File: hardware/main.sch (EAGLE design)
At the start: 107 parts, among them IC1 MPU-6050, IC2 TB6612FNG, M1 MOTOR_MOUNT_V2, M2 LED_MOUNT, M3 LED_MOUNT, M4 LED_MOUNT, M5 LED_MOUNT, M6 LED_MOUNT, M7 LED_MOUNT, Q7 IRLML2244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

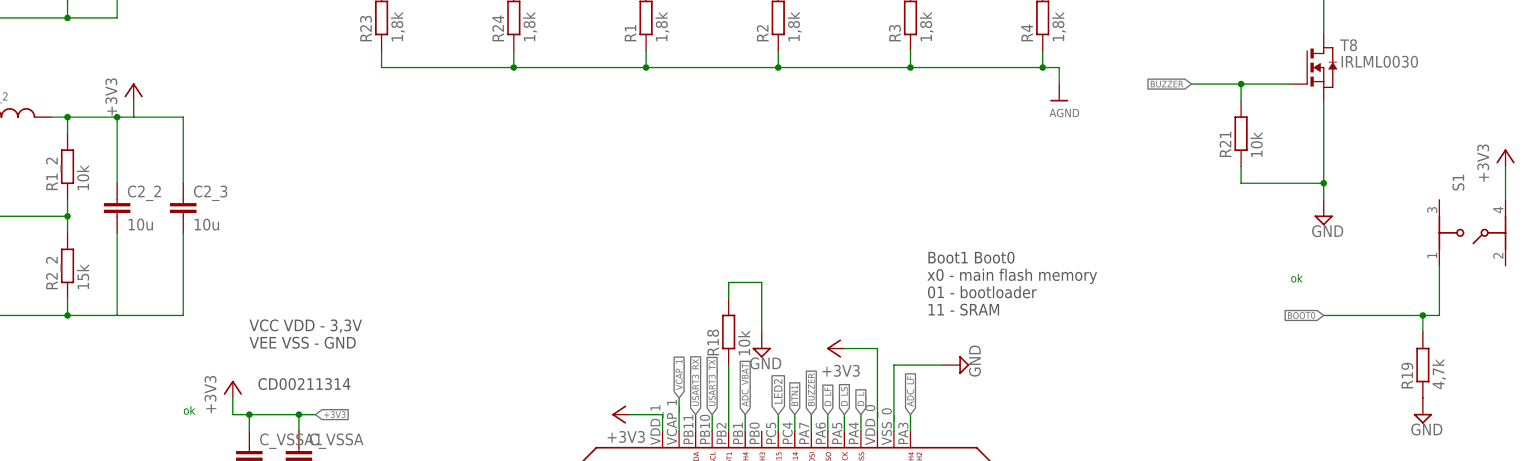
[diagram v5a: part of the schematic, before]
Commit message: pcb matches the 3d model
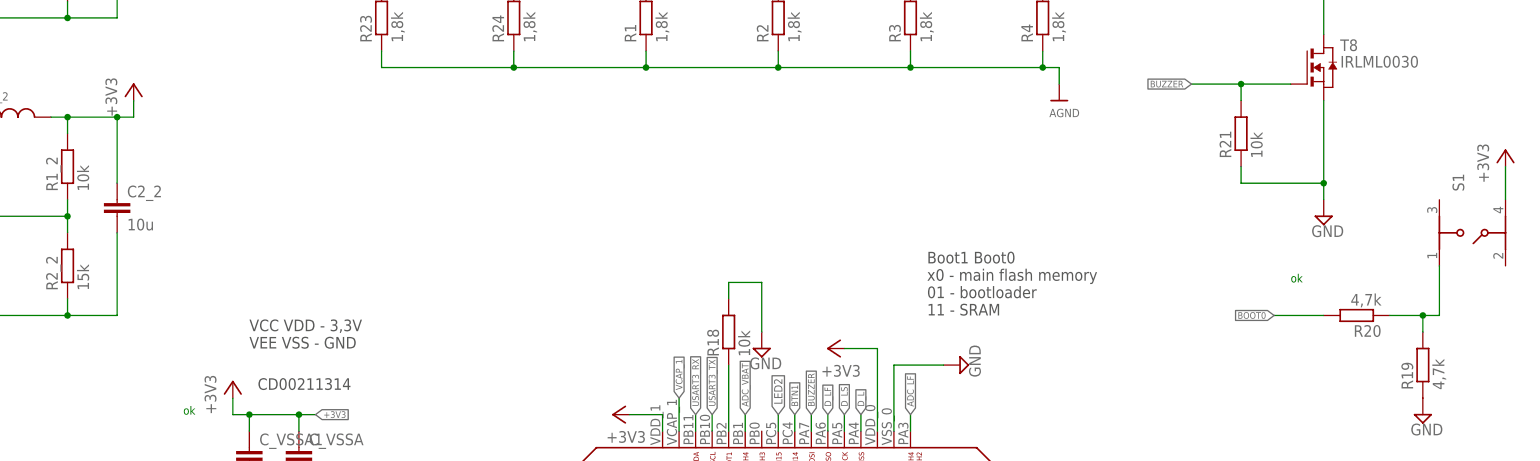
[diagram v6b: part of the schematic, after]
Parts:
- removed C2_3: 10u, rcl:C-EUC0805
- added R20: 4,7k, rcl:R-EU_R0603
- C1_3, C2_1, C2_2: device rcl:C-EUC0805 -> rcl:C-EUC1206
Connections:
- new net ASDF: R19.2, R20.1, S1.1
- net +3V3: no longer C2_3.1
- net BOOT0: now also R20.2; no longer R19.2, S1.1
- net GND: no longer C2_3.2

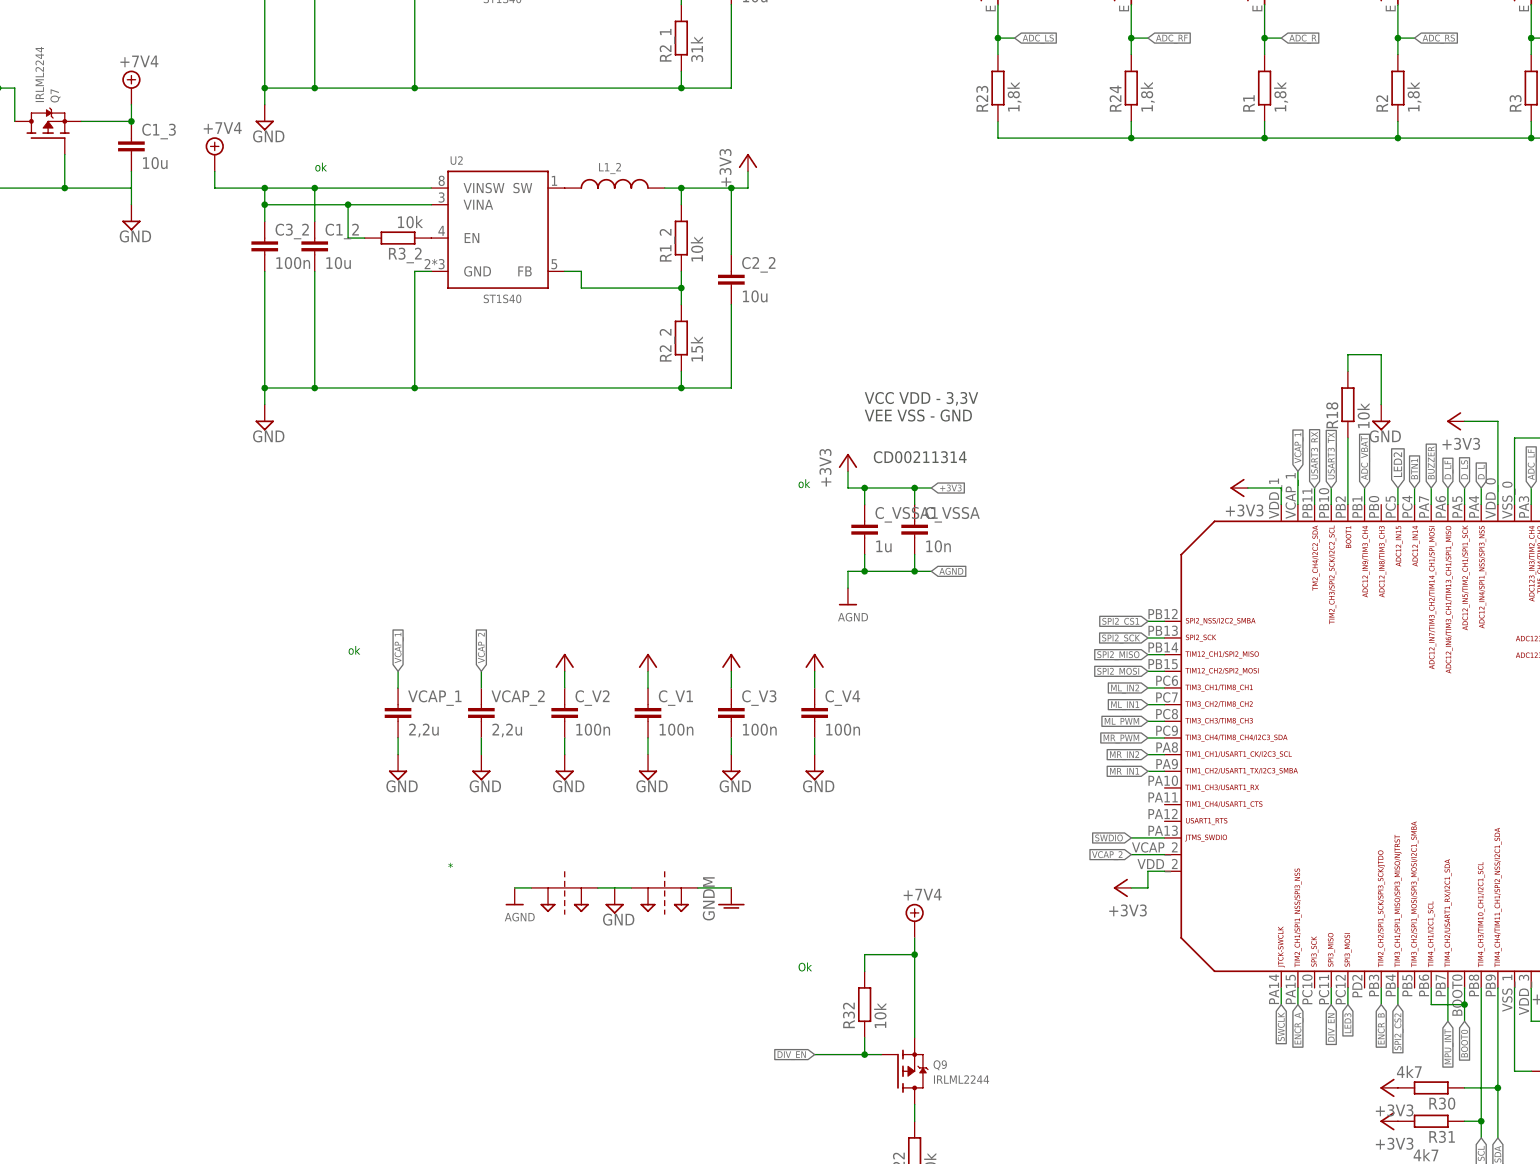
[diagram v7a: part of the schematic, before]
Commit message: moved step down converters closer to battery
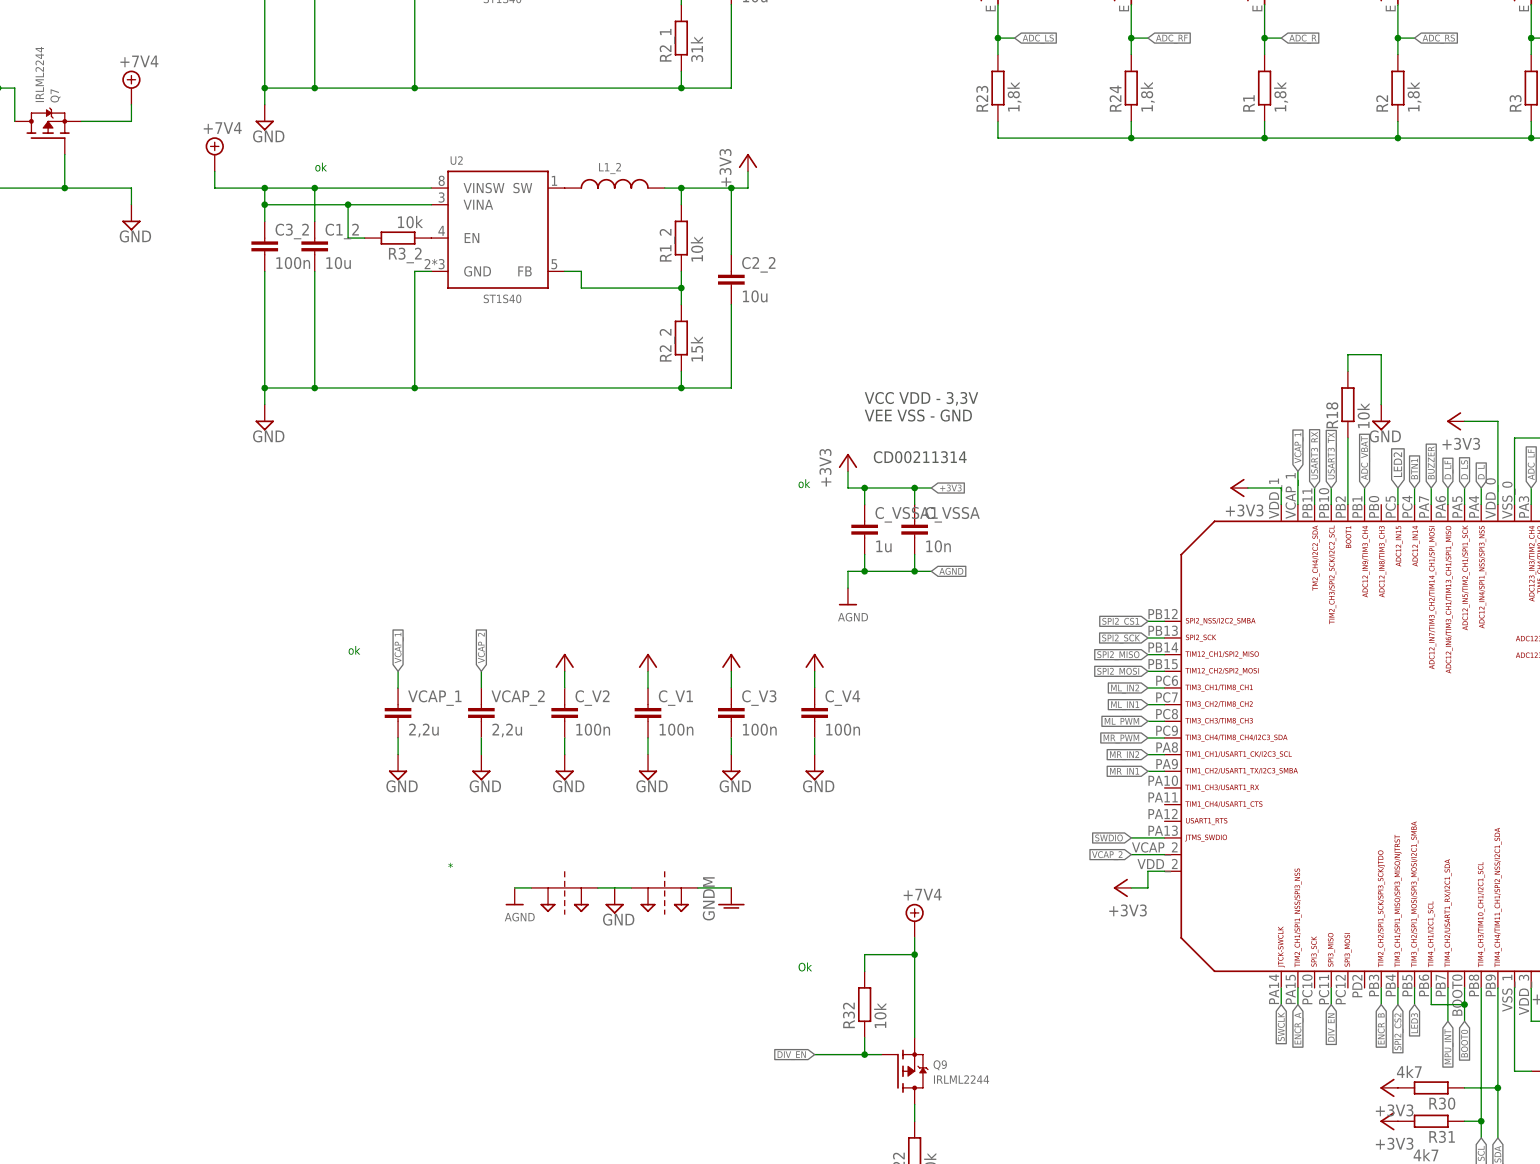
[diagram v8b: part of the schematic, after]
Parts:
- removed C1_3: 10u, rcl:C-EUC1206
- renumbered ON to OFF
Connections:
- net +7V: no longer C1_3.1
- net GND: no longer C1_3.2
- net LED3: now also U3.PB5; no longer U3.PC12
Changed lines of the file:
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@@
 <part name="GND1" library="supply1" deviceset="GNDA" device="" value="GNDM"/>
 <part name="Q7" library="microbuilder" deviceset="MOSFET-P" device="" value="IRLML2244"/>
-<part name="ON" library="micromouse" deviceset="PRZELACZNIK_SUWAKOWY" device=""/>
+<part name="OFF" library="micromouse" deviceset="PRZELACZNIK_SUWAKOWY" device=""/>
 <part name="R22" library="resistor" deviceset="R-EU_" device="R0603" value="10k"/>
 <part name="R25" library="resistor" deviceset="R-EU_" device="R0603" value="15k"/>
@@
 <part name="AGND1" library="supply2" deviceset="GND" device=""/>
 <part name="+3V28" library="supply1" deviceset="+3V3" device=""/>
-<part name="C1_3" library="rcl" deviceset="C-EU" device="C1206" value="10u"/>
 <part name="R8" library="rcl" deviceset="R-EU_" device="R0603" value="10k"/>
 <part name="R10" library="rcl" deviceset="R-EU_" device="R0603" value="10k"/>
@@
 <instance part="GND1" gate="1" x="86.36" y="325.12"/>
 <instance part="Q7" gate="G$1" x="-157.48" y="142.24" rot="MR90"/>
-<instance part="ON" gate="G$1" x="-172.72" y="147.32" rot="R270"/>
+<instance part="OFF" gate="G$1" x="-172.72" y="147.32" rot="R270"/>
 <instance part="R22" gate="G$1" x="-25.4" y="-15.24" rot="R90"/>
 <instance part="R25" gate="G$1" x="-25.4" y="-30.48" rot="R90"/>
@@
 <instance part="AGND1" gate="GND" x="137.16" y="-20.32"/>
 <instance part="+3V28" gate="G$1" x="137.16" y="5.08"/>
-<instance part="C1_3" gate="G$1" x="-144.78" y="139.7"/>
 <instance part="R8" gate="G$1" x="-22.86" y="200.66" rot="R90"/>
 <instance part="R10" gate="G$1" x="12.7" y="200.66" rot="R90"/>
@@
 <junction x="-154.94" y="132.08"/>
 <pinref part="JP2" gate="G$1" pin="1"/>
-<pinref part="C1_3" gate="G$1" pin="2"/>
-<wire x1="-144.78" y1="134.62" x2="-144.78" y2="132.08" width="0.1524" layer="91"/>
 </segment>
 <segment>
@@
 <net name="N$43" class="0">
 <segment>
-<pinref part="ON" gate="G$1" pin="2"/>
+<pinref part="OFF" gate="G$1" pin="2"/>
 <wire x1="-167.64" y1="147.32" x2="-165.1" y2="147.32" width="0.1524" layer="91"/>
 <wire x1="-165.1" y1="147.32" x2="-165.1" y2="149.86" width="0.1524" layer="91"/>
@@
 <wire x1="-162.56" y1="147.32" x2="-165.1" y2="147.32" width="0.1524" layer="91"/>
 <junction x="-165.1" y="147.32"/>
-<pinref part="ON" gate="G$1" pin="5"/>
+<pinref part="OFF" gate="G$1" pin="5"/>
 <wire x1="-177.8" y1="147.32" x2="-180.34" y2="147.32" width="0.1524" layer="91"/>
 <wire x1="-180.34" y1="147.32" x2="-180.34" y2="149.86" width="0.1524" layer="91"/>
@@
 <net name="N$46" class="0">
 <segment>
-<pinref part="ON" gate="G$1" pin="6"/>
+<pinref part="OFF" gate="G$1" pin="6"/>
 <wire x1="-177.8" y1="142.24" x2="-180.34" y2="142.24" width="0.1524" layer="91"/>
 <wire x1="-180.34" y1="142.24" x2="-180.34" y2="144.78" width="0.1524" layer="91"/>
 <wire x1="-180.34" y1="144.78" x2="-165.1" y2="144.78" width="0.1524" layer="91"/>
 <wire x1="-165.1" y1="144.78" x2="-165.1" y2="142.24" width="0.1524" layer="91"/>
-<pinref part="ON" gate="G$1" pin="3"/>
+<pinref part="OFF" gate="G$1" pin="3"/>
 <wire x1="-165.1" y1="142.24" x2="-167.64" y2="142.24" width="0.1524" layer="91"/>
 <pinref part="JP1" gate="G$1" pin="2"/>
@@
 <pinref part="Q7" gate="G$1" pin="S"/>
 <wire x1="-152.4" y1="142.24" x2="-144.78" y2="142.24" width="0.1524" layer="91"/>
-<pinref part="C1_3" gate="G$1" pin="1"/>
-<junction x="-144.78" y="142.24"/>
 </segment>
 <segment>
@@
 </segment>
 <segment>
-<pinref part="U3" gate="G$1" pin="PC12"/>
-<wire x1="40.64" y1="10.16" x2="40.64" y2="7.62" width="0.1524" layer="91"/>
-<label x="40.64" y="7.62" size="1.016" layer="95" rot="R270" xref="yes"/>
-</segment>
-</net>
+<pinref part="U3" gate="G$1" pin="PB5"/>
+<wire x1="50.8" y1="10.16" x2="50.8" y2="7.62" width="0.1524" layer="91"/>
+<label x="50.8" y="7.62" size="1.016" layer="95" rot="R270" xref="yes"/>
+</segment>
+</net>
